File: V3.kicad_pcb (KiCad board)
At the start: 2 copper layers, 128.2 x 61 mm, 109 parts, among them IC1 TPS62840DLCR","TPS62840DLCR, J1 Conn_01x04, J2 Conn_01x04, J3 FFC2B28-24-G, J4 Conn_01x04, J6 Conn_01x02, J7 Conn_01x02, Q3 FDN304P","FDN304P, Q4 FDN304P","FDN304P, Q8 SI1308EDL","SI1308EDL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

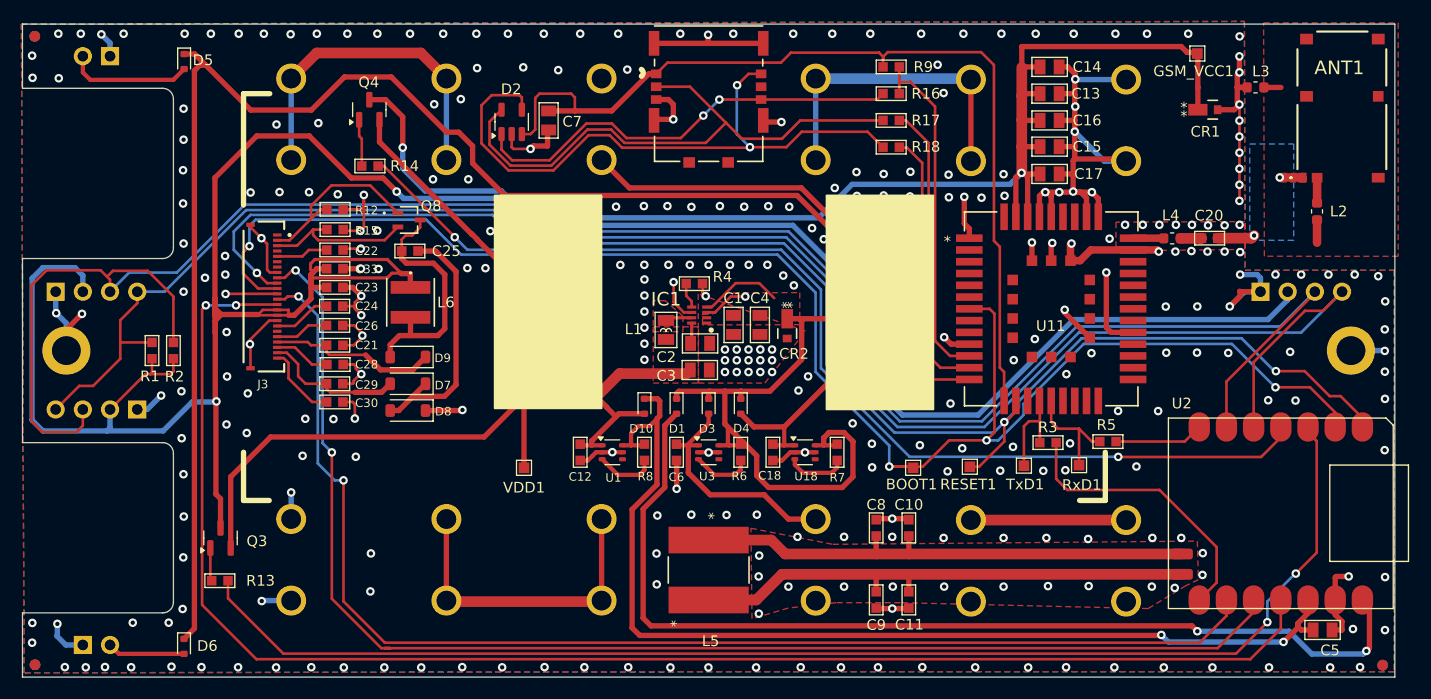
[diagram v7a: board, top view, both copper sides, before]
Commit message: clean up silk screen
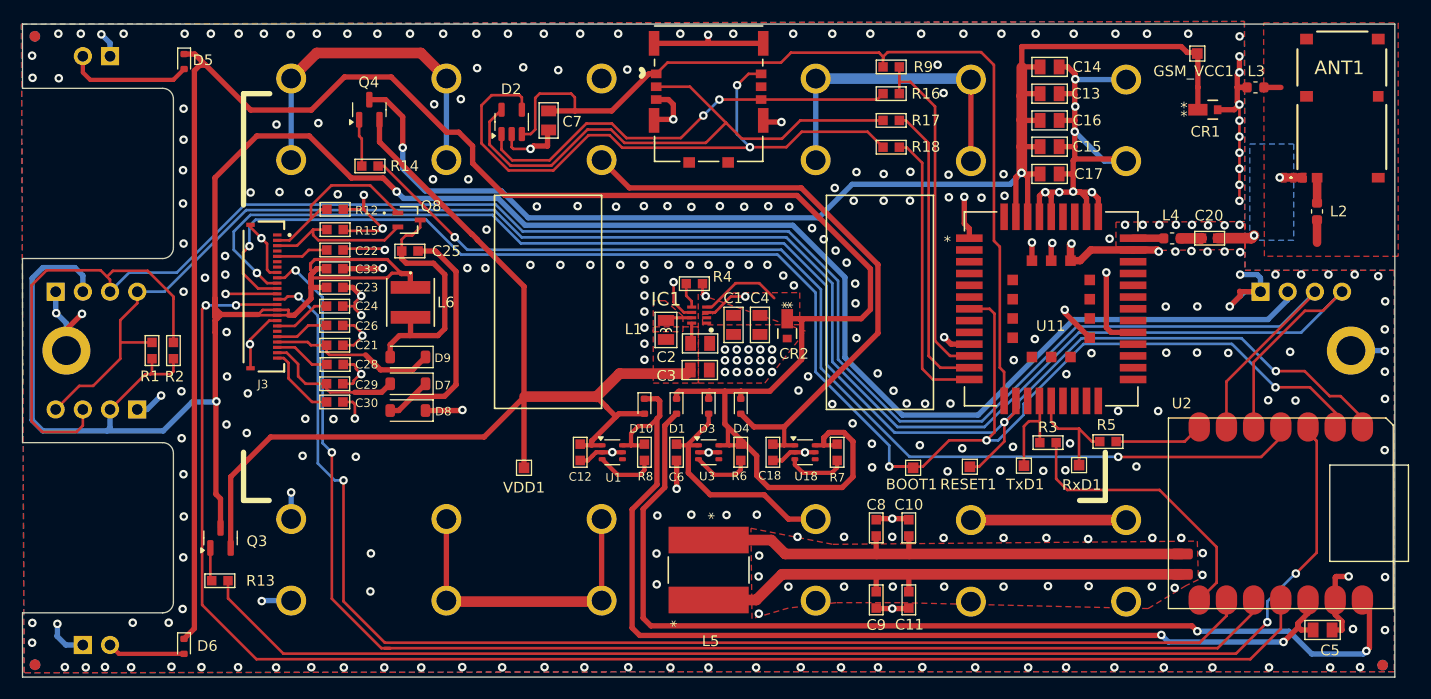
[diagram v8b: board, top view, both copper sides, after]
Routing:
- net GND: track 241.6 -> 248.5 mm, vias 333 -> 331
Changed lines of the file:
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@@
 		(tags "inductor")
 		(property "Reference" "L3"
-			(at -0.5 1.5 0)
+			(at -0.067 1.5154 0)
 			(layer "F.SilkS")
 			(effects
@@
 			(type solid)
 		)
-		(fill solid)
+		(fill none)
 		(layer "F.SilkS")
 	)
@@
 			(type solid)
 		)
-		(fill solid)
+		(fill none)
 		(layer "F.SilkS")
 	)
@@
 	)
 	(segment
+		(start -32.21 -13.16)
+		(end -32.21 -14.54)
+		(width 0.25)
+		(layer "F.Cu")
+		(net 75)
+	)
+	(segment
 		(start 49.583 -21.4846)
 		(end 49.583 -22.9846)
@@
 	)
 	(segment
-		(start 34.05 -14.8)
-		(end 34.05 -14.85)
-		(width 0.5)
+		(start -30.45 -11.4)
+		(end -32.21 -13.16)
+		(width 0.25)
 		(layer "F.Cu")
 		(net 75)
 	)
 	(segment
-		(start -32.48 -7.65)
-		(end -34.163 -7.65)
+		(start 34.05 -14.8)
+		(end 34.05 -14.85)
 		(width 0.5)
 		(layer "F.Cu")
@@
 	)
 	(segment
-		(start -32.53 -11.19)
-		(end -34.026998 -11.19)
-		(width 0.25)
-		(layer "F.Cu")
-		(net 75)
-	)
-	(segment
 		(start -42.8 -0.55)
 		(end -42.8 1.65)
@@
 	)
 	(segment
+		(start -30.66 -11.19)
+		(end -34.026998 -11.19)
+		(width 0.25)
+		(layer "F.Cu")
+		(net 75)
+	)
+	(segment
 		(start 33.9 -10)
 		(end 33.8 -9.9)
@@
 	)
 	(segment
+		(start -30.5 -7.65)
+		(end -34.163 -7.65)
+		(width 0.5)
+		(layer "F.Cu")
+		(net 75)
+	)
+	(segment
 		(start -33.1 -4.15)
 		(end -33.05 -4.1)
@@
 	)
 	(segment
-		(start -32.21 -14.54)
-		(end -32.21 -11.51)
-		(width 0.25)
-		(layer "F.Cu")
-		(net 75)
-	)
-	(segment
 		(start 24.35 -11.4)
 		(end 24.35 -10.500002)
@@
 	)
 	(segment
-		(start -32.49 -9.52)
-		(end -34.029999 -9.52)
-		(width 0.25)
-		(layer "F.Cu")
-		(net 75)
-	)
-	(segment
 		(start -1.5874 -3.5656)
 		(end -2.3124 -3.5656)
@@
 	)
 	(segment
+		(start -30.37 -9.52)
+		(end -34.029999 -9.52)
+		(width 0.25)
+		(layer "F.Cu")
+		(net 75)
+	)
+	(segment
 		(start 32 -14.4)
 		(end 31.6 -14.8)
@@
 	)
 	(segment
+		(start -30.45 -7.7)
+		(end -30.5 -7.65)
+		(width 0.5)
+		(layer "F.Cu")
+		(net 75)
+	)
+	(segment
 		(start 23.88 -11.87)
 		(end 24.35 -11.4)
@@
 	)
 	(segment
+		(start -30.25 -9.4)
+		(end -30.37 -9.52)
+		(width 0.25)
+		(layer "F.Cu")
+		(net 75)
+	)
+	(segment
 		(start 8.05 9.5)
 		(end 7.62 9.5)
@@
 	)
 	(segment
-		(start -32.21 -11.51)
-		(end -32.53 -11.19)
+		(start -30.45 -11.4)
+		(end -30.66 -11.19)
 		(width 0.25)
 		(layer "F.Cu")
@@
 	)
 	(via
-		(at -30.84 -7.62)
-		(size 0.8)
-		(drill 0.4)
-		(layers "F.Cu" "B.Cu")
-		(free yes)
-		(net 75)
-	)
-	(via
 		(at 32.1 -10.05)
 		(size 0.8)
@@
 	)
 	(via
-		(at 18.81 -14.4)
+		(at 18.81 -14)
 		(size 0.8)
 		(drill 0.4)
@@
 	)
 	(via
-		(at -32.53 -11.19)
+		(at -30.45 -11.4)
 		(size 0.8)
 		(drill 0.4)
@@
 	)
 	(via
-		(at -30.95 -11.2)
-		(size 0.8)
-		(drill 0.4)
-		(layers "F.Cu" "B.Cu")
-		(free yes)
-		(net 75)
-	)
-	(via
 		(at 31.45 -14.8)
 		(size 0.8)
@@
 	)
 	(via
-		(at -32.49 -9.52)
+		(at -30.25 -9.4)
 		(size 0.8)
 		(drill 0.4)
@@
 	)
 	(via
-		(at 13.85 -14.45)
+		(at 13.55 -14)
 		(size 0.8)
 		(drill 0.4)
@@
 	)
 	(via
-		(at -32.48 -7.65)
+		(at -30.45 -7.7)
 		(size 0.8)
 		(drill 0.4)
@@
 	)
 	(via
-		(at 16.35 -14.49)
+		(at 16.35 -14)
 		(size 0.8)
 		(drill 0.4)
@@
 	)
 	(via
-		(at -20.39 -11.16)
+		(at -20.75 -11.3)
 		(size 0.8)
 		(drill 0.4)
